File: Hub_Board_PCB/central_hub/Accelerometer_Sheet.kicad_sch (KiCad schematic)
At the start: 4 parts, among them U3 MPU-6050

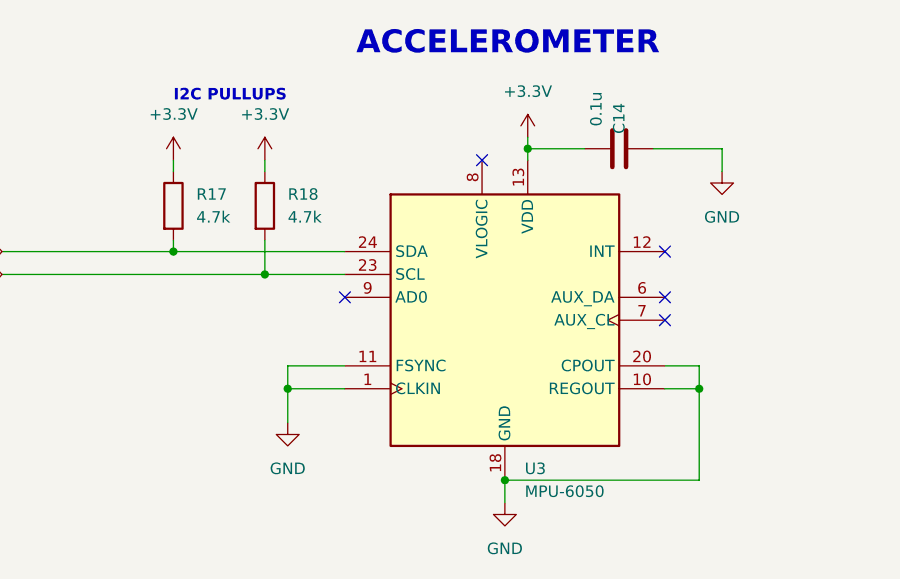
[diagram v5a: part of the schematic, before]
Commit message: - fixed capacitor values on MCU sheet (both central hub and motor board) - added missing Accelerometer componenets - changed BOOT HEADER (both central hub and motor board) - set the Arduino "love" signal to NC - fixed overlapping pins on USB connector
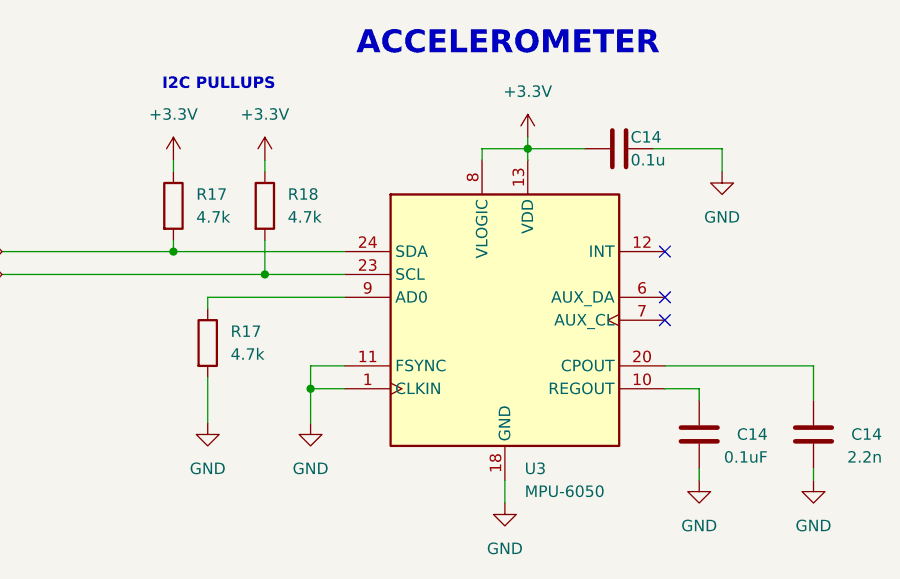
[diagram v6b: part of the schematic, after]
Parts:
- added C14: 0.1uF, Capacitor_SMD:C_0603_1608Metric, symbol Device:C
- added C14: 2.2n, Capacitor_SMD:C_0603_1608Metric, symbol Device:C
- added R17: 4.7k, Resistor_SMD:R_0603_1608Metric, symbol Device:R
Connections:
- net +3.3V: now also U3.8 (VLOGIC)
- net GND: now also C14.1, C14.1, R17.2; no longer U3.10 (REGOUT), U3.20 (CPOUT)
- net at U3.9 (AD0): now also R17.1
- new net: C14.2, U3.10 (REGOUT)
- new net: C14.2, U3.20 (CPOUT)
- no-connect marks 5 -> 3

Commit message: Schematic changes before sending to kim
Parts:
- added C14: 10n, Capacitor_SMD:C_0603_1608Metric, symbol Device:C
- added R18 (x2): 4.7k, Resistor_SMD:R_0603_1608Metric, symbol Device:R
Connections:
- net +3.3V: now also C14.1
- net GND: now also C14.2, R18.2, R18.2; no longer U3.1 (CLKIN), U3.11 (FSYNC)
- new net: R18.1, U3.11 (FSYNC)
- new net: R18.1, U3.1 (CLKIN)
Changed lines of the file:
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@@
 (kicad_sch (version 20230121) (generator eeschema)
   (paper "A4")
-  (junction (at 132.08 107.95) (diameter 0) (color 0 0 0 0)
+  (junction (at 151.13 81.28) (diameter 0) (color 0 0 0 0)
   )
   (junction (at 156.21 81.28) (diameter 0) (color 0 0 0 0)
@@
   )
   (junction (at 127 95.25) (diameter 0) (color 0 0 0 0)
+  )
+  (junction (at 132.08 123.19) (diameter 0) (color 0 0 0 0)
   )
   (no_connect (at 171.45 100.33))
@@
     (stroke (width 0) (type default))
   )
-  (wire (pts (xy 132.08 107.95) (xy 132.08 111.76))
+  (wire (pts (xy 137.16 81.28) (xy 137.16 83.82))
     (stroke (width 0) (type default))
   )
@@
     (stroke (width 0) (type default))
   )
-  (wire (pts (xy 132.08 105.41) (xy 132.08 107.95))
+  (wire (pts (xy 128.27 121.92) (xy 128.27 123.19))
+    (stroke (width 0) (type default))
+  )
+  (wire (pts (xy 128.27 105.41) (xy 128.27 114.3))
     (stroke (width 0) (type default))
   )
@@
     (stroke (width 0) (type default))
   )
-  (wire (pts (xy 135.89 105.41) (xy 132.08 105.41))
-    (stroke (width 0) (type default))
-  )
   (wire (pts (xy 97.79 92.71) (xy 116.84 92.71))
     (stroke (width 0) (type default))
@@
     (stroke (width 0) (type default))
   )
+  (wire (pts (xy 132.08 121.92) (xy 132.08 123.19))
+    (stroke (width 0) (type default))
+  )
   (wire (pts (xy 162.56 81.28) (xy 156.21 81.28))
     (stroke (width 0) (type default))
@@
     (stroke (width 0) (type default))
   )
+  (wire (pts (xy 132.08 123.19) (xy 132.08 124.46))
+    (stroke (width 0) (type default))
+  )
   (wire (pts (xy 127 91.44) (xy 127 95.25))
     (stroke (width 0) (type default))
   )
+  (wire (pts (xy 135.89 105.41) (xy 128.27 105.41))
+    (stroke (width 0) (type default))
+  )
   (wire (pts (xy 177.8 81.28) (xy 177.8 83.82))
     (stroke (width 0) (type default))
@@
     (stroke (width 0) (type default))
   )
+  (wire (pts (xy 128.27 123.19) (xy 132.08 123.19))
+    (stroke (width 0) (type default))
+  )
   (wire (pts (xy 116.84 92.71) (xy 135.89 92.71))
     (stroke (width 0) (type default))
   )
-  (wire (pts (xy 135.89 107.95) (xy 132.08 107.95))
+  (wire (pts (xy 138.43 81.28) (xy 137.16 81.28))
     (stroke (width 0) (type default))
   )
@@
     (stroke (width 0) (type default))
   )
+  (wire (pts (xy 146.05 81.28) (xy 151.13 81.28))
+    (stroke (width 0) (type default))
+  )
   (wire (pts (xy 171.45 105.41) (xy 187.96 105.41))
     (stroke (width 0) (type default))
   )
+  (wire (pts (xy 132.08 107.95) (xy 135.89 107.95))
+    (stroke (width 0) (type default))
+  )
   (wire (pts (xy 175.26 116.84) (xy 175.26 118.11))
+    (stroke (width 0) (type default))
+  )
+  (wire (pts (xy 132.08 114.3) (xy 132.08 107.95))
     (stroke (width 0) (type default))
   )
@@
     )
   )
-  (symbol (lib_id "power:GND") (at 132.08 111.76 0) (unit 1)
-    (in_bom yes) (on_board yes) (dnp no) (fields_autoplaced)
-    (property "Reference" "#PWR042" (at 132.08 118.11 0)
-      (effects (font (size 1.27 1.27)) hide)
-    )
-    (property "Value" "GND" (at 132.08 116.84 0)
-      (effects (font (size 1.27 1.27)))
-    )
-    (property "Footprint" "" (at 132.08 111.76 0)
-      (effects (font (size 1.27 1.27)) hide)
-    )
-    (property "Datasheet" "" (at 132.08 111.76 0)
+  (symbol (lib_id "power:GND") (at 132.08 124.46 0) (unit 1)
+    (in_bom yes) (on_board yes) (dnp no) (fields_autoplaced)
+    (property "Reference" "#PWR042" (at 132.08 130.81 0)
+      (effects (font (size 1.27 1.27)) hide)
+    )
+    (property "Value" "GND" (at 132.08 129.54 0)
+      (effects (font (size 1.27 1.27)))
+    )
+    (property "Footprint" "" (at 132.08 124.46 0)
+      (effects (font (size 1.27 1.27)) hide)
+    )
+    (property "Datasheet" "" (at 132.08 124.46 0)
       (effects (font (size 1.27 1.27)) hide)
     )
@@
         (path "/0d9ec66e-0fbf-4d12-9b83-adf78971a00b/406a2e52-8680-458b-82c4-a5b80d2a411b"
           (reference "#PWR072") (unit 1)
+        )
+      )
+    )
+  )
+  (symbol (lib_id "power:GND") (at 137.16 83.82 0) (unit 1)
+    (in_bom yes) (on_board yes) (dnp no) (fields_autoplaced)
+    (property "Reference" "#PWR042" (at 137.16 90.17 0)
+      (effects (font (size 1.27 1.27)) hide)
+    )
+    (property "Value" "GND" (at 137.16 88.9 0)
+      (effects (font (size 1.27 1.27)))
+    )
+    (property "Footprint" "" (at 137.16 83.82 0)
+      (effects (font (size 1.27 1.27)) hide)
+    )
+    (property "Datasheet" "" (at 137.16 83.82 0)
+      (effects (font (size 1.27 1.27)) hide)
+    )
+    (pin "1")
+    (instances
+      (project "central_hub"
+        (path "/0d9ec66e-0fbf-4d12-9b83-adf78971a00b"
+          (reference "#PWR042") (unit 1)
+        )
+        (path "/0d9ec66e-0fbf-4d12-9b83-adf78971a00b/4fb60496-ee10-4e45-a75e-a49c2c8afc68"
+          (reference "#PWR0119") (unit 1)
+        )
+        (path "/0d9ec66e-0fbf-4d12-9b83-adf78971a00b/406a2e52-8680-458b-82c4-a5b80d2a411b"
+          (reference "#PWR058") (unit 1)
         )
       )
@@
     )
   )
+  (symbol (lib_id "Device:R") (at 128.27 118.11 0) (unit 1)
+    (in_bom yes) (on_board yes) (dnp no) (fields_autoplaced)
+    (property "Reference" "R18" (at 130.81 116.84 0)
+      (effects (font (size 1.27 1.27)) (justify left))
+    )
+    (property "Value" "4.7k" (at 130.81 119.38 0)
+      (effects (font (size 1.27 1.27)) (justify left))
+    )
+    (property "Footprint" "Resistor_SMD:R_0603_1608Metric" (at 126.492 118.11 90)
+      (effects (font (size 1.27 1.27)) hide)
+    )
+    (property "Datasheet" "~" (at 128.27 118.11 0)
+      (effects (font (size 1.27 1.27)) hide)
+    )
+    (pin "1")
+    (pin "2")
+    (instances
+      (project "central_hub"
+        (path "/0d9ec66e-0fbf-4d12-9b83-adf78971a00b"
+          (reference "R18") (unit 1)
+        )
+        (path "/0d9ec66e-0fbf-4d12-9b83-adf78971a00b/4fb60496-ee10-4e45-a75e-a49c2c8afc68"
+          (reference "R32") (unit 1)
+        )
+        (path "/0d9ec66e-0fbf-4d12-9b83-adf78971a00b/406a2e52-8680-458b-82c4-a5b80d2a411b"
+          (reference "R34") (unit 1)
+        )
+      )
+    )
+  )
   (symbol (lib_id "power:GND") (at 187.96 118.11 0) (unit 1)
     (in_bom yes) (on_board yes) (dnp no) (fields_autoplaced)
@@
         (path "/0d9ec66e-0fbf-4d12-9b83-adf78971a00b/406a2e52-8680-458b-82c4-a5b80d2a411b"
           (reference "#PWR032") (unit 1)
+        )
+      )
+    )
+  )
+  (symbol (lib_id "Device:R") (at 132.08 118.11 0) (unit 1)
+    (in_bom yes) (on_board yes) (dnp no) (fields_autoplaced)
+    (property "Reference" "R18" (at 134.62 116.84 0)
+      (effects (font (size 1.27 1.27)) (justify left))
+    )
+    (property "Value" "4.7k" (at 134.62 119.38 0)
+      (effects (font (size 1.27 1.27)) (justify left))
+    )
+    (property "Footprint" "Resistor_SMD:R_0603_1608Metric" (at 130.302 118.11 90)
+      (effects (font (size 1.27 1.27)) hide)
+    )
+    (property "Datasheet" "~" (at 132.08 118.11 0)
+      (effects (font (size 1.27 1.27)) hide)
+    )
+    (pin "1")
+    (pin "2")
+    (instances
+      (project "central_hub"
+        (path "/0d9ec66e-0fbf-4d12-9b83-adf78971a00b"
+          (reference "R18") (unit 1)
+        )
+        (path "/0d9ec66e-0fbf-4d12-9b83-adf78971a00b/4fb60496-ee10-4e45-a75e-a49c2c8afc68"
+          (reference "R32") (unit 1)
+        )
+        (path "/0d9ec66e-0fbf-4d12-9b83-adf78971a00b/406a2e52-8680-458b-82c4-a5b80d2a411b"
+          (reference "R33") (unit 1)
         )
       )
@@
         )
       )
+    )
+  )
+  (symbol (lib_id "Device:C") (at 142.24 81.28 270) (unit 1)
+    (in_bom yes) (on_board yes) (dnp no)
+    (property "Reference" "C14" (at 143.51 80.01 90)
+      (effects (font (size 1.27 1.27)) (justify left))
+    )
+    (property "Value" "10n" (at 143.51 82.55 90)
+      (effects (font (size 1.27 1.27)) (justify left))
+    )
+    (property "Footprint" "Capacitor_SMD:C_0603_1608Metric" (at 138.43 82.2452 0)
+      (effects (font (size 1.27 1.27)) hide)
+    )
+    (property "Datasheet" "~" (at 142.24 81.28 0)
+      (effects (font (size 1.27 1.27)) hide)
+    )
+    (pin "1")
+    (pin "2")
+    (instances
+      (project "central_hub"
+        (path "/0d9ec66e-0fbf-4d12-9b83-adf78971a00b/a9a7affa-d8a7-4dcd-8fe3-0de6a2b29bd6"
+          (reference "C14") (unit 1)
+        )
+        (path "/0d9ec66e-0fbf-4d12-9b83-adf78971a00b/406a2e52-8680-458b-82c4-a5b80d2a411b"
+          (reference "C31") (unit 1)
+        )
+      )
+      (project "motor_board_pcb"
+        (path "/4ad82a24-c992-45c9-b523-12e12bcd6ced"
+          (reference "C?") (unit 1)
+        )
+        (path "/4ad82a24-c992-45c9-b523-12e12bcd6ced/63c66207-e5d4-4f6f-af8f-451675dc3930"
+          (reference "C14") (unit 1)
+        )
+      )

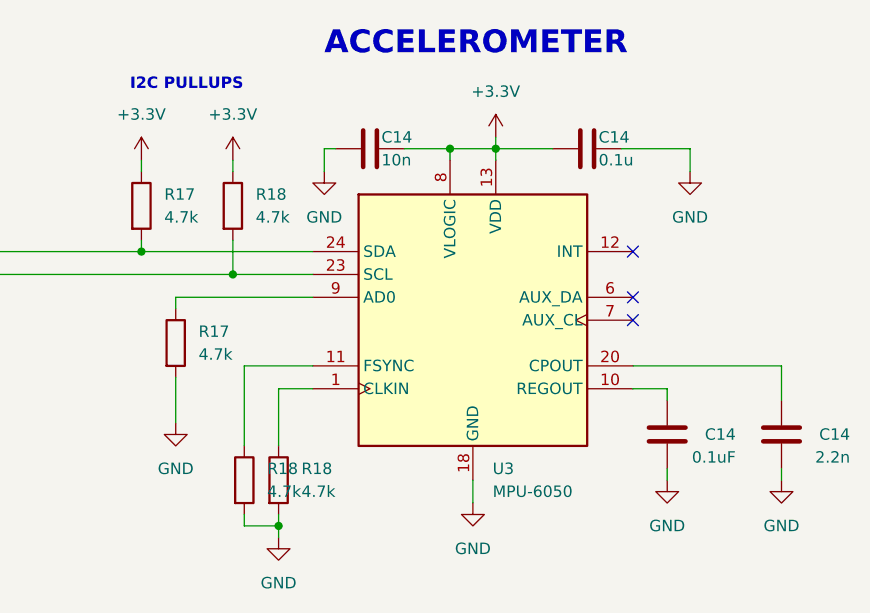
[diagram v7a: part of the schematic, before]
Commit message: - added footprint labels to schematic
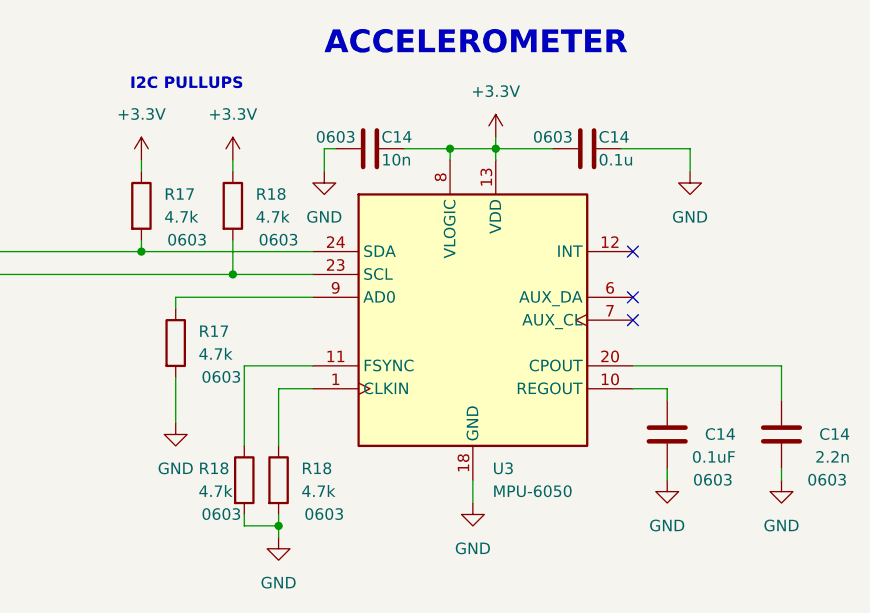
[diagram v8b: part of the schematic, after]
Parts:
- C14, R17, R18: FP (none) -> 0603
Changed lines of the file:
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@@
   )
   (symbol (lib_id "Device:R") (at 127 87.63 0) (unit 1)
-    (in_bom yes) (on_board yes) (dnp no) (fields_autoplaced)
+    (in_bom yes) (on_board yes) (dnp no)
     (property "Reference" "R18" (at 129.54 86.36 0)
       (effects (font (size 1.27 1.27)) (justify left))
@@
     (property "Datasheet" "~" (at 127 87.63 0)
       (effects (font (size 1.27 1.27)) hide)
+    )
+    (property "FP" "0603" (at 132.08 91.44 0)
+      (effects (font (size 1.27 1.27)))
     )
     (pin "1")
@@
       (effects (font (size 1.27 1.27)) hide)
     )
+    (property "FP" "0603" (at 162.56 80.01 90)
+      (effects (font (size 1.27 1.27)))
+    )
     (pin "1")
     (pin "2")
@@
   )
   (symbol (lib_id "Device:R") (at 116.84 87.63 0) (unit 1)
-    (in_bom yes) (on_board yes) (dnp no) (fields_autoplaced)
+    (in_bom yes) (on_board yes) (dnp no)
     (property "Reference" "R17" (at 119.38 86.36 0)
       (effects (font (size 1.27 1.27)) (justify left))
@@
       (effects (font (size 1.27 1.27)) hide)
     )
+    (property "FP" "0603" (at 121.92 91.44 0)
+      (effects (font (size 1.27 1.27)))
+    )
     (pin "1")
     (pin "2")
@@
   )
   (symbol (lib_id "Device:R") (at 128.27 118.11 0) (unit 1)
-    (in_bom yes) (on_board yes) (dnp no) (fields_autoplaced)
-    (property "Reference" "R18" (at 130.81 116.84 0)
-      (effects (font (size 1.27 1.27)) (justify left))
-    )
-    (property "Value" "4.7k" (at 130.81 119.38 0)
+    (in_bom yes) (on_board yes) (dnp no)
+    (property "Reference" "R18" (at 123.19 116.84 0)
+      (effects (font (size 1.27 1.27)) (justify left))
+    )
+    (property "Value" "4.7k" (at 123.19 119.38 0)
       (effects (font (size 1.27 1.27)) (justify left))
     )
@@
     (property "Datasheet" "~" (at 128.27 118.11 0)
       (effects (font (size 1.27 1.27)) hide)
+    )
+    (property "FP" "0603" (at 125.73 121.92 0)
+      (effects (font (size 1.27 1.27)))
     )
     (pin "1")
@@
   )
   (symbol (lib_id "Device:R") (at 132.08 118.11 0) (unit 1)
-    (in_bom yes) (on_board yes) (dnp no) (fields_autoplaced)
+    (in_bom yes) (on_board yes) (dnp no)
     (property "Reference" "R18" (at 134.62 116.84 0)
       (effects (font (size 1.27 1.27)) (justify left))
@@
       (effects (font (size 1.27 1.27)) hide)
     )
+    (property "FP" "0603" (at 137.16 121.92 0)
+      (effects (font (size 1.27 1.27)))
+    )
     (pin "1")
     (pin "2")
@@
   )
   (symbol (lib_id "Device:R") (at 120.65 102.87 0) (unit 1)
-    (in_bom yes) (on_board yes) (dnp no) (fields_autoplaced)
+    (in_bom yes) (on_board yes) (dnp no)
     (property "Reference" "R17" (at 123.19 101.6 0)
       (effects (font (size 1.27 1.27)) (justify left))
@@
       (effects (font (size 1.27 1.27)) hide)
     )
+    (property "FP" "0603" (at 125.73 106.68 0)
+      (effects (font (size 1.27 1.27)))
+    )
     (pin "1")
     (pin "2")
@@
     (property "Datasheet" "~" (at 175.26 113.03 0)
       (effects (font (size 1.27 1.27)) hide)
+    )
+    (property "FP" "0603" (at 180.34 118.11 0)
+      (effects (font (size 1.27 1.27)))
     )
     (pin "1")
@@
       (effects (font (size 1.27 1.27)) hide)
     )
+    (property "FP" "0603" (at 193.04 118.11 0)
+      (effects (font (size 1.27 1.27)))
+    )
     (pin "1")
     (pin "2")
@@
       (effects (font (size 1.27 1.27)) hide)
     )
-    (pin "1")
+    (property "FP" "0603" (at 138.43 80.01 90)
+      (effects (font (size 1.27 1.27)))
+    )
+    (pin "1")
